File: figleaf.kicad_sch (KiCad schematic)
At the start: 41 parts, among them U1 Nice_Nano_V2_GRAZ, U2 XIAO-nRF52840-Plus-SMD

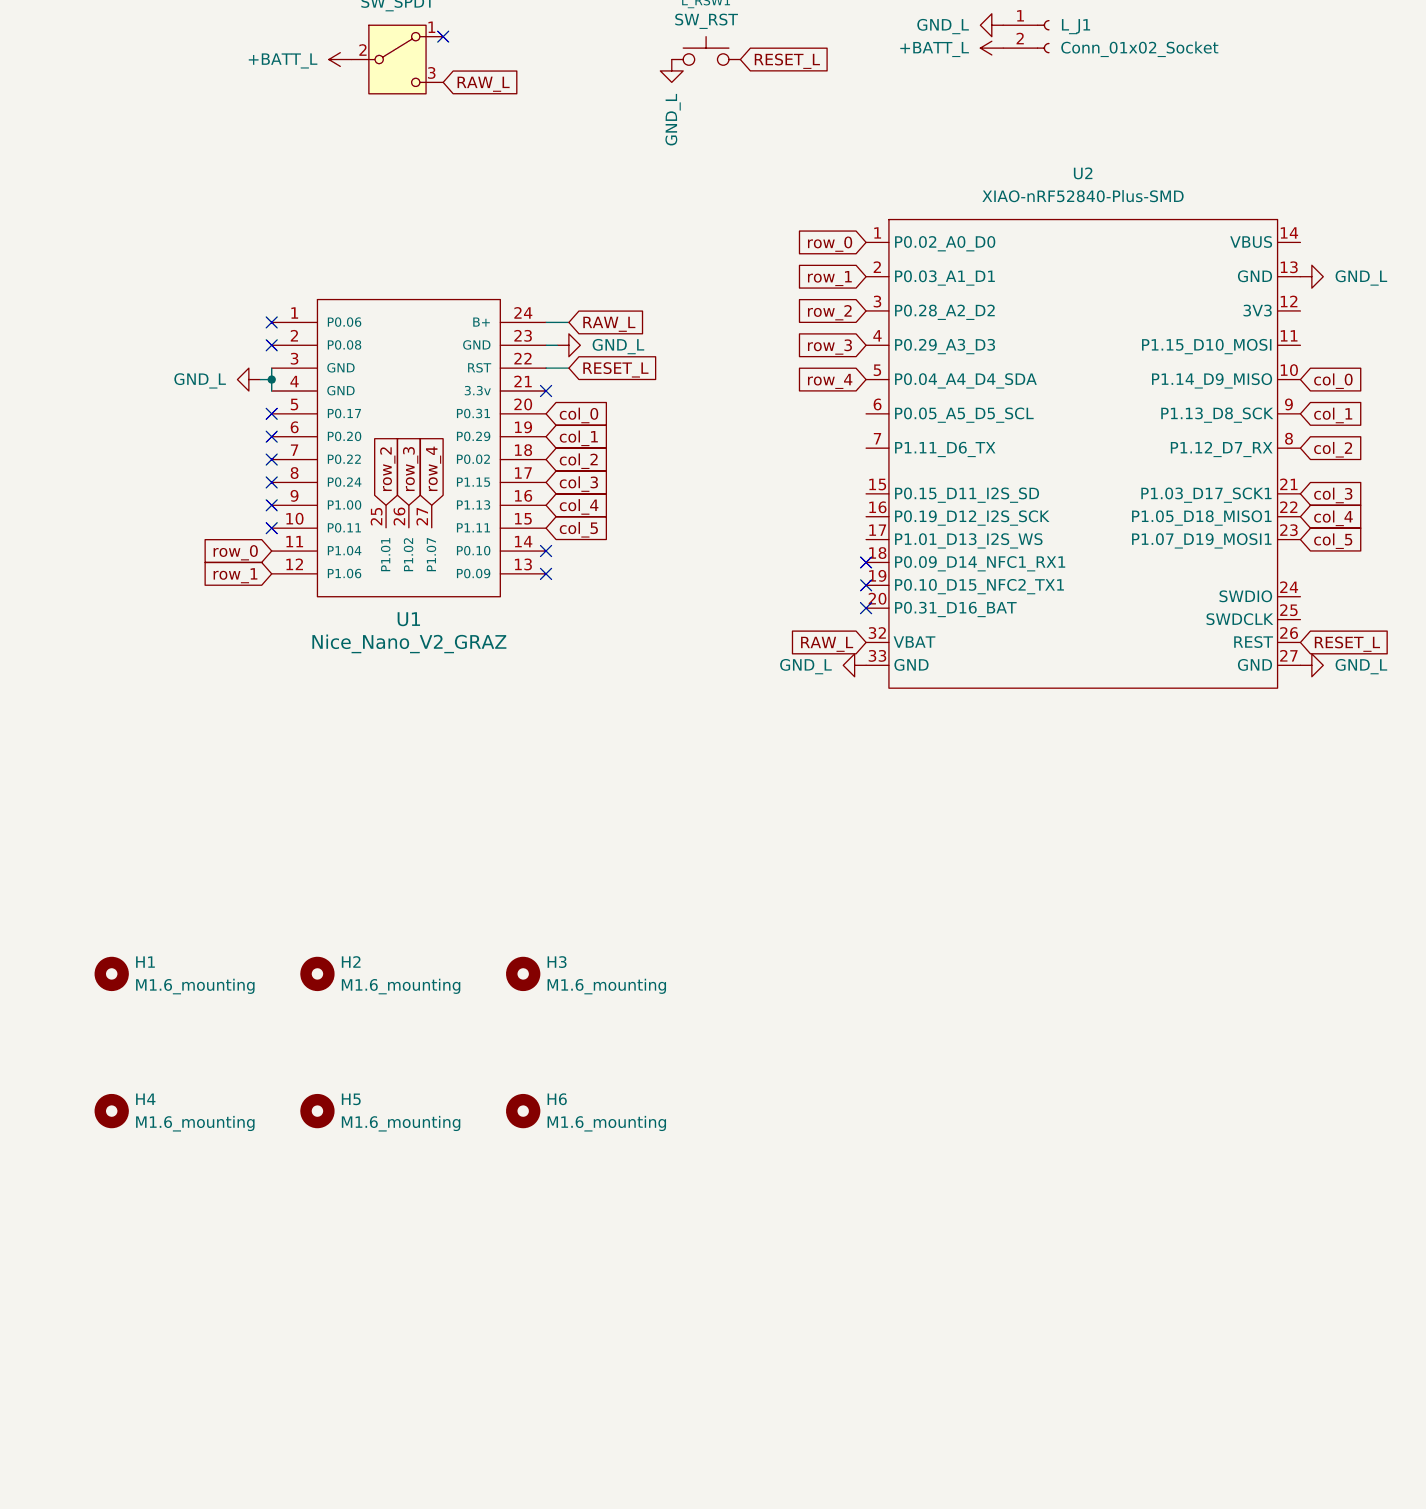
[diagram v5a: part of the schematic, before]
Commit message: new xiao MCU progress
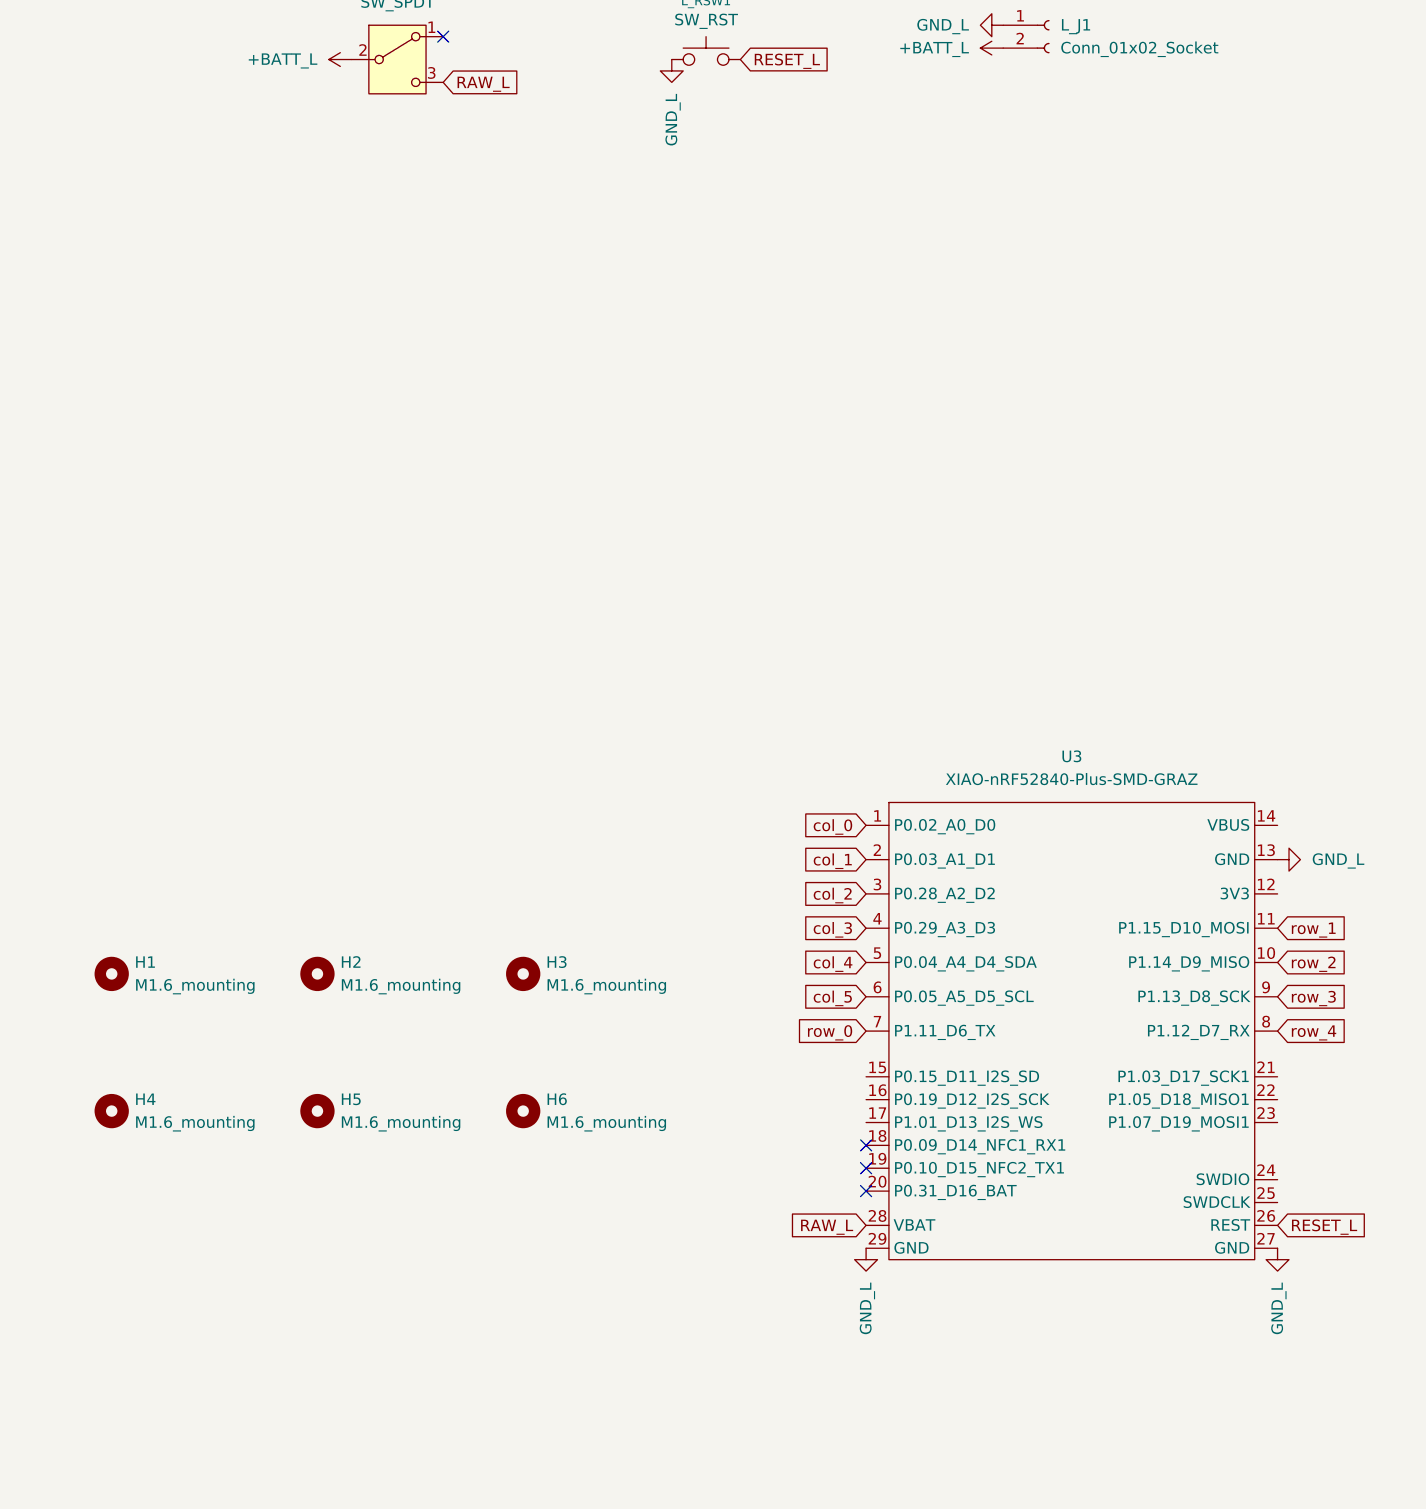
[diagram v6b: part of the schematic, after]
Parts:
- removed U1: Nice_Nano_V2_GRAZ, Graz_Footprints:Nice_Nano_V2_Graz, symbol 0_graz_symbols:MCU_Nice_Nano_V2
- removed U2: XIAO-nRF52840-Plus-SMD, Graz_Footprints:XIAO-nRF52840-Plus-SMD, symbol 0_graz_symbols:XIAO-nRF52840_Plus_SMD
- added U3: XIAO-nRF52840-Plus-SMD-GRAZ, Graz_Footprints:XIAO-nRF52840-Plus-SMD, symbol 0_graz_symbols:XIAO-nRF52840_Plus_SMD_GRAZ
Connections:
- net GND_L: now also U3.13 (GND), U3.27 (GND), U3.29 (GND)
- net RAW_L: now also U3.28 (VBAT)
- net RESET_L: now also U3.26 (REST)
- net col_0: now also U3.1 (P0.02_A0_D0)
- net col_1: now also U3.2 (P0.03_A1_D1)
- net col_2: now also U3.3 (P0.28_A2_D2)
- net col_3: now also U3.4 (P0.29_A3_D3)
- net col_4: now also U3.5 (P0.04_A4_D4_SDA)
- net col_5: now also U3.6 (P0.05_A5_D5_SCL)
- net row_0: now also U3.7 (P1.11_D6_TX)
- net row_1: now also U3.11 (P1.15_D10_MOSI)
- net row_2: now also U3.10 (P1.14_D9_MISO)
- net row_3: now also U3.9 (P1.13_D8_SCK)
- net row_4: now also U3.8 (P1.12_D7_RX)
- no-connect marks 26 -> 15

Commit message: flip progress 1
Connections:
- net col_0: now also U3.11 (P1.15_D10_MOSI); no longer U3.1 (P0.02_A0_D0)
- net col_1: now also U3.10 (P1.14_D9_MISO); no longer U3.2 (P0.03_A1_D1)
- net col_2: now also U3.9 (P1.13_D8_SCK); no longer U3.3 (P0.28_A2_D2)
- net col_3: now also U3.8 (P1.12_D7_RX); no longer U3.4 (P0.29_A3_D3)
- net col_4: now also U3.7 (P1.11_D6_TX); no longer U3.5 (P0.04_A4_D4_SDA)
- net row_0: now also U3.5 (P0.04_A4_D4_SDA); no longer U3.7 (P1.11_D6_TX)
- net row_1: now also U3.4 (P0.29_A3_D3); no longer U3.11 (P1.15_D10_MOSI)
- net row_2: now also U3.3 (P0.28_A2_D2); no longer U3.10 (P1.14_D9_MISO)
- net row_3: now also U3.2 (P0.03_A1_D1); no longer U3.9 (P1.13_D8_SCK)
- net row_4: now also U3.1 (P0.02_A0_D0); no longer U3.8 (P1.12_D7_RX)
